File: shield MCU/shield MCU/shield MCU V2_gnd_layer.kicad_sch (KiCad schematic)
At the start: 16 parts, among them J1 IR_sensor, J2 IR_sensor, J3 IR_sensor, J4 IR_sensor, J5 IR_sensor, J6 BATT, SW1 Pwr_Sw, U1 pwr_mgr_1, U3 gy50, U4 NUCLEO144-F429ZI

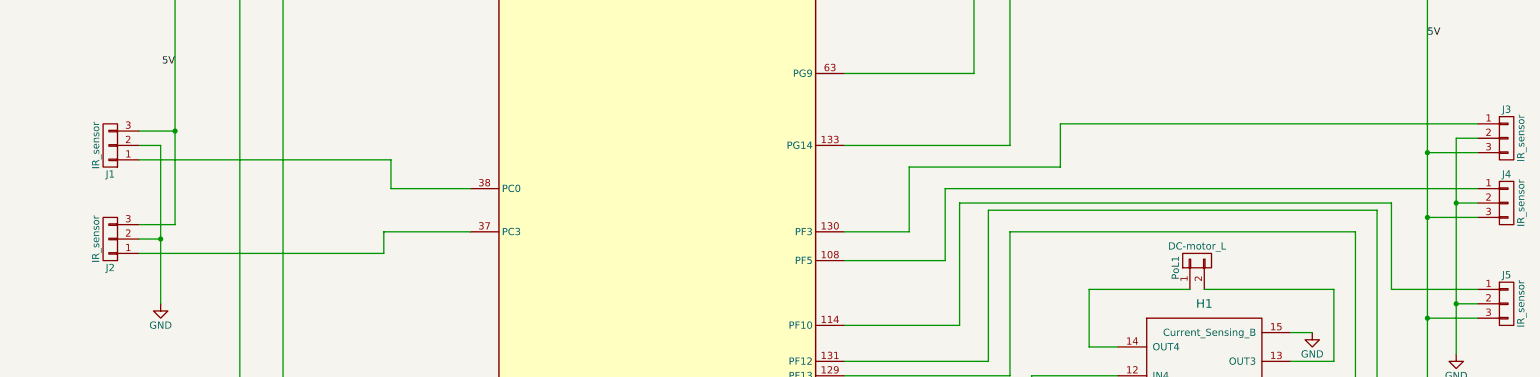
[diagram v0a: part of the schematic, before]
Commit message: PCB päivitetty
switchien VIA koot muutettu ja L298N footprint päivitetty
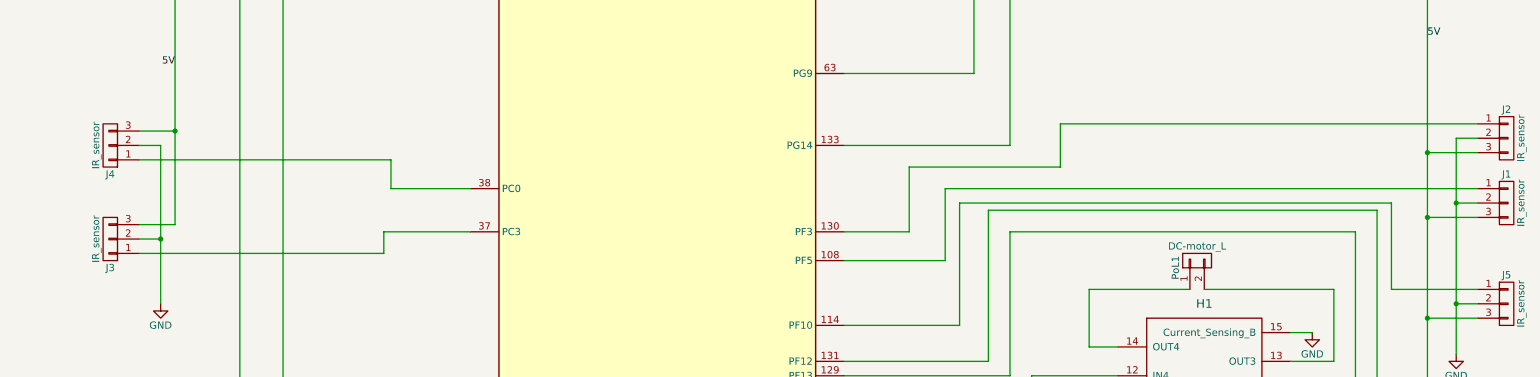
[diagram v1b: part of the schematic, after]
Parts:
- renumbered J4 to J1, J3 to J2, J2 to J3, J1 to J4
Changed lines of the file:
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@@
   (symbol (lib_id "ardu_auto2_0-rescue:CONN_01X03-Arduino_shield-rescue") (at 308.61 146.05 0) (unit 1)
     (in_bom yes) (on_board yes)
-    (property "Reference" "J3" (id 0) (at 308.61 140.97 0))
+    (property "Reference" "J2" (id 0) (at 308.61 140.97 0))
     (property "Value" "IR_sensor" (id 1) (at 311.15 146.05 90))
     (property "Footprint" "Connector_PinHeader_2.54mm:PinHeader_1x03_P2.54mm_Vertical" (id 2) (at 308.61 146.05 0)
@@
   (symbol (lib_id "ardu_auto2_0-rescue:CONN_01X03-Arduino_shield-rescue") (at 62.23 163.83 180) (unit 1)
     (in_bom yes) (on_board yes)
-    (property "Reference" "J2" (id 0) (at 62.23 168.91 0))
+    (property "Reference" "J3" (id 0) (at 62.23 168.91 0))
     (property "Value" "IR_sensor" (id 1) (at 59.69 163.83 90))
     (property "Footprint" "Connector_PinHeader_2.54mm:PinHeader_1x03_P2.54mm_Vertical" (id 2) (at 62.23 163.83 0)
@@
   (symbol (lib_id "ardu_auto2_0-rescue:CONN_01X03-Arduino_shield-rescue") (at 62.23 147.32 180) (unit 1)
     (in_bom yes) (on_board yes)
-    (property "Reference" "J1" (id 0) (at 62.23 152.4 0))
+    (property "Reference" "J4" (id 0) (at 62.23 152.4 0))
     (property "Value" "IR_sensor" (id 1) (at 59.69 147.32 90))
     (property "Footprint" "Connector_PinHeader_2.54mm:PinHeader_1x03_P2.54mm_Vertical" (id 2) (at 62.23 147.32 0)
@@
   (symbol (lib_id "ardu_auto2_0-rescue:CONN_01X03-Arduino_shield-rescue") (at 308.61 157.48 0) (unit 1)
     (in_bom yes) (on_board yes)
-    (property "Reference" "J4" (id 0) (at 308.61 152.4 0))
+    (property "Reference" "J1" (id 0) (at 308.61 152.4 0))
     (property "Value" "IR_sensor" (id 1) (at 311.15 157.48 90))
     (property "Footprint" "Connector_PinHeader_2.54mm:PinHeader_1x03_P2.54mm_Vertical" (id 2) (at 308.61 157.48 0)
@@
       (reference "H1") (unit 1) (value "Half-bridge") (footprint "Omat:L298HN")
     )
+    (path "/cafb3204-9631-4c62-99c6-5dc6baad06e2"
+      (reference "J1") (unit 1) (value "IR_sensor") (footprint "Connector_PinHeader_2.54mm:PinHeader_1x03_P2.54mm_Vertical")
+    )
+    (path "/230567c0-7caf-4639-bb34-b5eb4d53ac4c"
+      (reference "J2") (unit 1) (value "IR_sensor") (footprint "Connector_PinHeader_2.54mm:PinHeader_1x03_P2.54mm_Vertical")
+    )
+    (path "/7fda894a-de6b-4380-8e0a-e719ef440511"
+      (reference "J3") (unit 1) (value "IR_sensor") (footprint "Connector_PinHeader_2.54mm:PinHeader_1x03_P2.54mm_Vertical")
+    )
     (path "/96eb817a-341f-49a7-912e-92df87d08c00"
-      (reference "J1") (unit 1) (value "IR_sensor") (footprint "Connector_PinHeader_2.54mm:PinHeader_1x03_P2.54mm_Vertical")
-    )
-    (path "/7fda894a-de6b-4380-8e0a-e719ef440511"
-      (reference "J2") (unit 1) (value "IR_sensor") (footprint "Connector_PinHeader_2.54mm:PinHeader_1x03_P2.54mm_Vertical")
-    )
-    (path "/230567c0-7caf-4639-bb34-b5eb4d53ac4c"
-      (reference "J3") (unit 1) (value "IR_sensor") (footprint "Connector_PinHeader_2.54mm:PinHeader_1x03_P2.54mm_Vertical")
-    )
-    (path "/cafb3204-9631-4c62-99c6-5dc6baad06e2"
       (reference "J4") (unit 1) (value "IR_sensor") (footprint "Connector_PinHeader_2.54mm:PinHeader_1x03_P2.54mm_Vertical")
     )
